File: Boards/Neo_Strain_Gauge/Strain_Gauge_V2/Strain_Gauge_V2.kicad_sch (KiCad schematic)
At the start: 14 parts, among them J6 USB_B_Micro, J7 Conn_02x10_Counter_Clockwise, J8 Conn_02x12_Counter_Clockwise, U2 NCP1117-3.3_SOT223, U6 AZ1117-5.0, U9 AP2112K-1.8

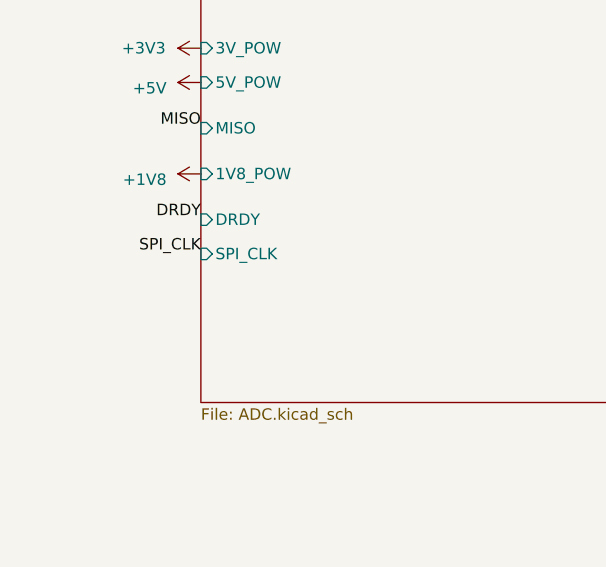
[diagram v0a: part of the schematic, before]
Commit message: Update board to use two voltage references
This will be a "demo" for a two-reference board, next I will most likely
design one with a differential instrumentation amplifier before
having a new board with 4 instrumentation amplifiers and a single-ended
ADC involved.
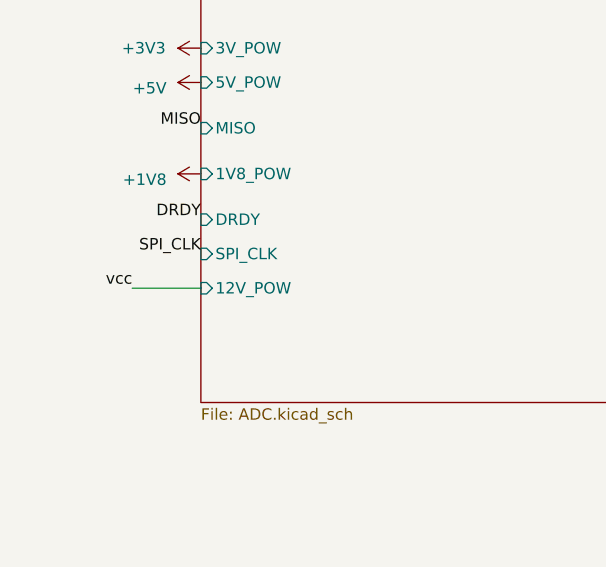
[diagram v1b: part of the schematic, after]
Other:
- sheet Analog Reader ports: added 12V_POW; removed none
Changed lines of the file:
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@@
+    (stroke (width 0) (type default))
+  )
+  (wire (pts (xy 38.1 80.01) (xy 45.72 80.01))
     (stroke (width 0) (type default))
   )
@@
   )
   (label "rpi_5v" (at 93.98 135.89 180) (fields_autoplaced)
+    (effects (font (size 1.27 1.27)) (justify right bottom))
+  )
+  (label "vcc" (at 38.1 80.01 180) (fields_autoplaced)
     (effects (font (size 1.27 1.27)) (justify right bottom))
   )
@@
       (effects (font (size 1.27 1.27)) (justify left))
     )
+    (pin "12V_POW" input (at 45.72 80.01 180)
+      (effects (font (size 1.27 1.27)) (justify left))
+    )
